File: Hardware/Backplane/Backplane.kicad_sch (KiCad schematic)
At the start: 5 parts, among them U101 P2X8C4M64P, U102 TCA9548APWR

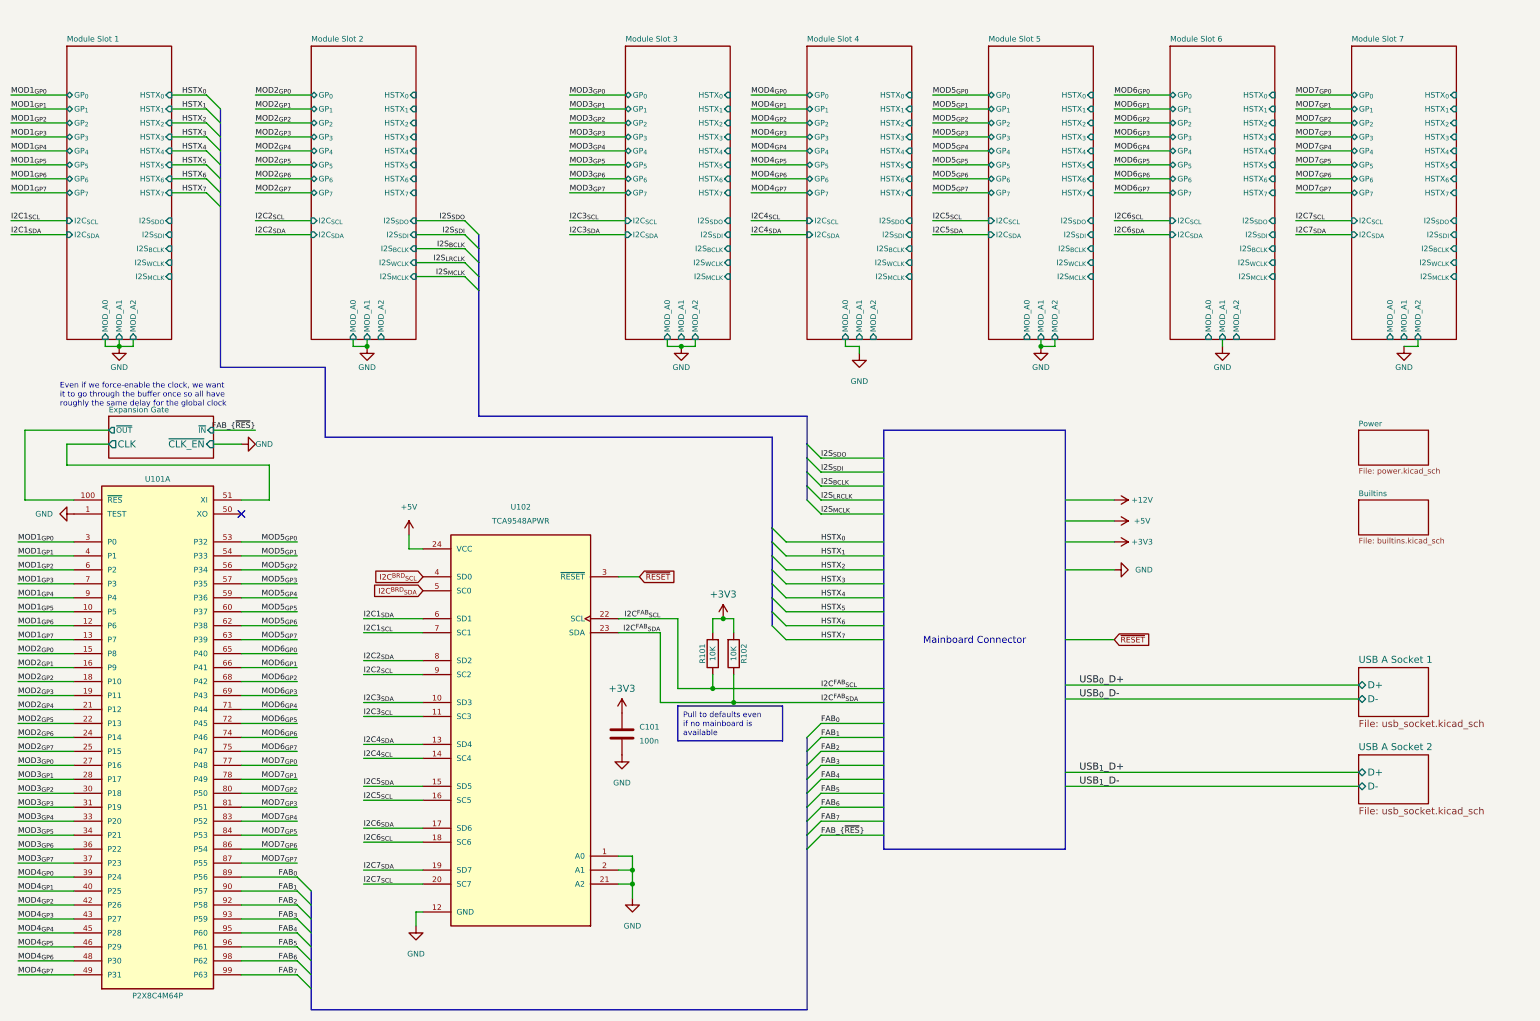
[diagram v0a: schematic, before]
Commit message: Refactors clock system to use AND gates for clock tree spanning and gating.
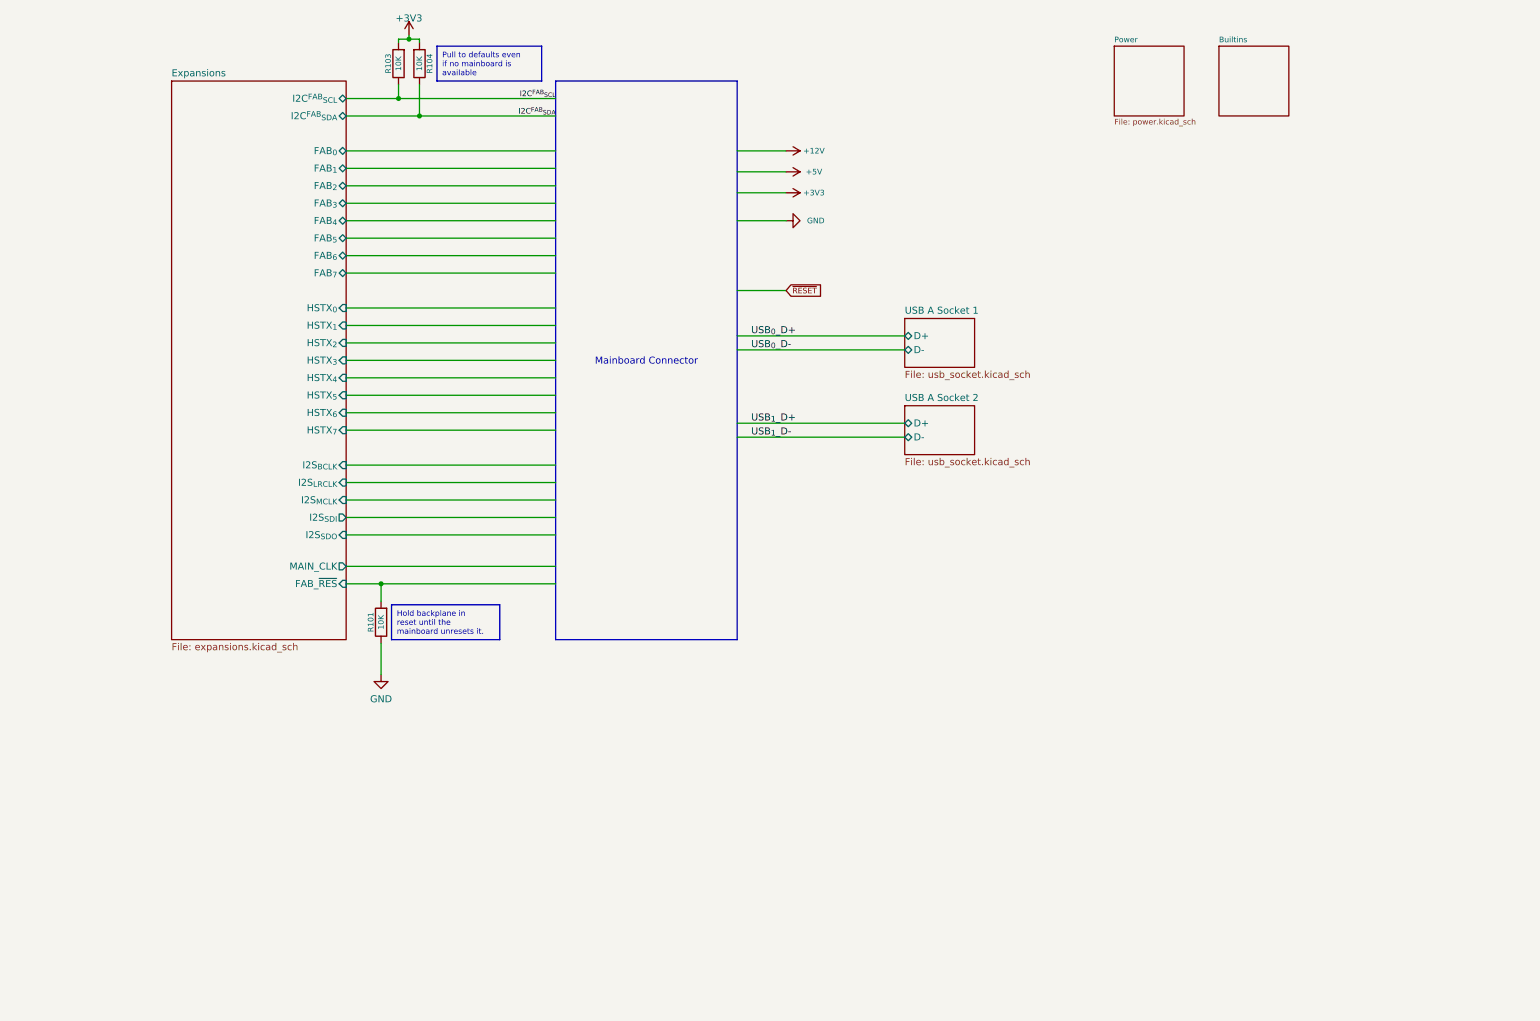
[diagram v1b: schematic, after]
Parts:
- removed C101: 100n, Capacitor_SMD:C_0603_1608Metric, symbol Device:C
- removed R102: 10K, Resistor_SMD:R_0603_1608Metric, symbol Device:R
- removed U101: P2X8C4M64P, Home Computer:QFP50P1600X1600X120-101N, symbol Home Computer:P2X8C4M64P
- removed U102: TCA9548APWR, TCA9548APWR:SOP65P640X120-24N, symbol Home Computer:TCA9548APWR
- added R103, R104: 10K, Resistor_SMD:R_0603_1608Metric, symbol Device:R
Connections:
- net +3V3: now also R103.2, R104.2; no longer R101.2
- net GND: now also R101.1
- net I2C^{FAB}_{SCL}: now also R103.1; no longer R101.1
- net I2C^{FAB}_{SDA}: now also R104.1
- new net Expansions/FAB_~{RES}: R101.2
- no-connect marks 1 -> 0
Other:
- removed sheet Expansion Gate
- removed sheet Module Slot 1
- removed sheet Module Slot 2
- removed sheet Module Slot 3
- removed sheet Module Slot 4
- removed sheet Module Slot 5
- removed sheet Module Slot 6
- removed sheet Module Slot 7
- added sheet Expansions (expansions.kicad_sch)
- note removed: "Even if we force-enable the clock, we want it to go through the buffer once so all have roughly the same delay for the global clock"

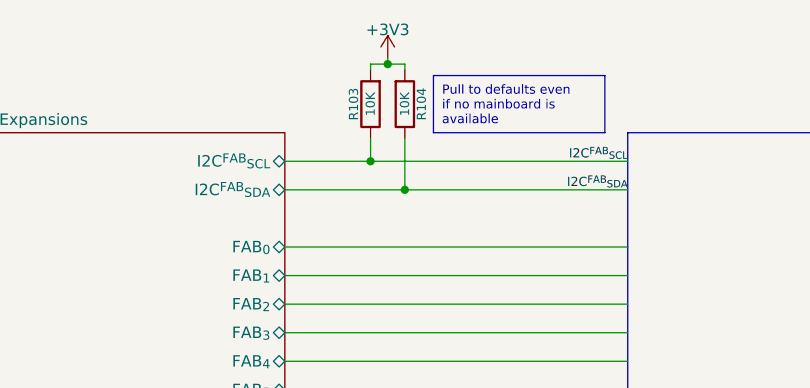
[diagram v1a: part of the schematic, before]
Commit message: Some cleanups of Backplane schematic: Adds DigiKey part numbers, removes unnecessary properties, marks test points as excluded from BOM
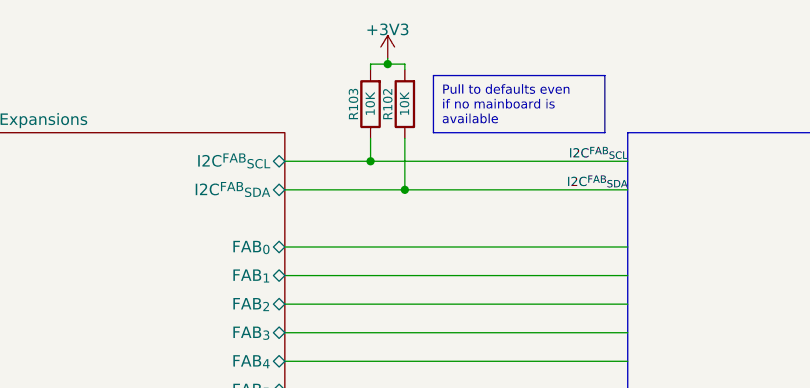
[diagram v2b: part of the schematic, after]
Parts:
- removed R104: 10K, Resistor_SMD:R_0603_1608Metric, symbol Device:R
- added R102: 10K, Resistor_SMD:R_0603_1608Metric, symbol Device:R
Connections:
- net +3V3: now also R102.2
- net I2C^{FAB}_{SDA}: now also R102.1
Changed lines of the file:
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@@
-	(symbol
-		(lib_id "Device:R")
-		(at 89.535 22.225 0)
-		(mirror x)
-		(unit 1)
-		(exclude_from_sim no)
-		(in_bom yes)
-		(on_board yes)
-		(dnp no)
-		(property "Reference" "R104"
-			(at 90.805 22.225 90)
-			(effects
-				(font
-					(size 1.016 1.016)
-				)
-				(justify top)
-			)
-		)
-		(property "Value" "10K"
-			(at 89.535 22.225 90)
-			(effects
-				(font
-					(size 1.016 1.016)
-				)
-			)
-		)
-		(property "Footprint" "Resistor_SMD:R_0603_1608Metric"
-			(at 87.757 22.225 90)
-			(effects
-				(font
-					(size 1.27 1.27)
-				)
-				(hide yes)
-			)
-		)
-		(property "Datasheet" "~"
-			(at 89.535 22.225 0)
-			(effects
-				(font
-					(size 1.27 1.27)
-				)
-				(hide yes)
-			)
-		)
-		(property "Description" "Resistor"
-			(at 89.535 22.225 0)
-			(effects
-				(font
-					(size 1.27 1.27)
-				)
-				(hide yes)
-			)
-		)
-		(pin "1"
-		)
-		(pin "2"
-		)
-		(instances
-			(project "Backplane"
-				(path "/c6da991a-d3ed-4ac1-8b0d-12cd7ba8539b"
-					(reference "R104")
-					(unit 1)
-				)
-			)
-		)
-	)
 	(symbol
 		(lib_id "Device:R")
@@
 			)
 		)
-		(property "Datasheet" "~"
+		(property "Datasheet" ""
 			(at 85.725 22.225 0)
 			(effects
@@
 			)
 		)
-		(property "Datasheet" "~"
+		(property "Datasheet" ""
 			(at 82.55 123.825 0)
 			(effects
@@
 					(unit 1)
 				)
+			)
+		)
+	)
+	(symbol
+		(lib_id "Device:R")
+		(at 89.535 22.225 180)
+		(unit 1)
+		(exclude_from_sim no)
+		(in_bom yes)
+		(on_board yes)
+		(dnp no)
+		(property "Reference" "R102"
+			(at 88.265 22.225 90)
+			(effects
+				(font
+					(size 1.016 1.016)
+				)
+				(justify top)
+			)
+		)
+		(property "Value" "10K"
+			(at 89.535 22.225 90)
+			(effects
+				(font
+					(size 1.016 1.016)
+				)
+			)
+		)
+		(property "Footprint" "Resistor_SMD:R_0603_1608Metric"
+			(at 91.313 22.225 90)
+			(effects
+				(font
+					(size 1.27 1.27)
+				)
+				(hide yes)
+			)
+		)
+		(property "Datasheet" ""
+			(at 89.535 22.225 0)
+			(effects
+				(font
+					(size 1.27 1.27)
+				)
+				(hide yes)
+			)
+		)
+		(property "Description" "Resistor"
+			(at 89.535 22.225 0)
+			(effects
+				(font
+					(size 1.27 1.27)
+				)
+				(hide yes)
+			)
+		)
+		(pin "1"
+		)
+		(pin "2"
+		)
+		(instances
+			(project "Backplane"
+				(path "/c6da991a-d3ed-4ac1-8b0d-12cd7ba8539b"
+					(reference "R102")
+					(unit 1)
+				)

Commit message: Adjusts to review comments
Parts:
- added J101: 10018784-10201TLF, Home Computer:CONN_10018784-10201TLF, symbol Home Computer:10018784-10201TLF
- R101, R102, R103: Digikey Part No (none) -> 311-10.0KHRCT-ND
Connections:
- net +12V: now also J101.B1
- net +3V3: now also J101.B5
- net +5V: now also J101.B3
- net Expansions/FAB_{0}: now also J101.A8
- net Expansions/FAB_{1}: now also J101.A9
- net Expansions/FAB_{2}: now also J101.A10
- net Expansions/FAB_{3}: now also J101.A11
- net Expansions/FAB_{4}: now also J101.A12
- net Expansions/FAB_{5}: now also J101.A13
- net Expansions/FAB_{6}: now also J101.A14
- net Expansions/FAB_{7}: now also J101.A15
- net Expansions/FAB_~{RES}: now also J101.A32
- net Expansions/HSTX_{0}: now also J101.A17
- net Expansions/HSTX_{1}: now also J101.A18
- net Expansions/HSTX_{2}: now also J101.A19
- net Expansions/HSTX_{3}: now also J101.A20
- net Expansions/HSTX_{4}: now also J101.A21
- net Expansions/HSTX_{5}: now also J101.A22
- net Expansions/HSTX_{6}: now also J101.A23
- net Expansions/HSTX_{7}: now also J101.A24
- net Expansions/I2S_{BCLK}: now also J101.A25
- net Expansions/I2S_{LRCLK}: now also J101.A26
- net Expansions/I2S_{MCLK}: now also J101.A27
- net Expansions/I2S_{SDI}: now also J101.A28
- net Expansions/I2S_{SDO}: now also J101.A29
- net Expansions/MAIN_CLK: now also J101.A31
- net GND: now also J101.B12, J101.B2, J101.B4, J101.B6, J101.B9
- net I2C^{FAB}_{SCL}: now also J101.A1
- net I2C^{FAB}_{SDA}: now also J101.A2
- net USB_{0}_D+: now also J101.B7
- net USB_{0}_D-: now also J101.B8
- net USB_{1}_D+: now also J101.B10
- net USB_{1}_D-: now also J101.B11
- net ~{RESET}: now also J101.A16
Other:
- note added: "Mainboard Connector"
- note added: "Programming Edge Conncetor for faster production?"

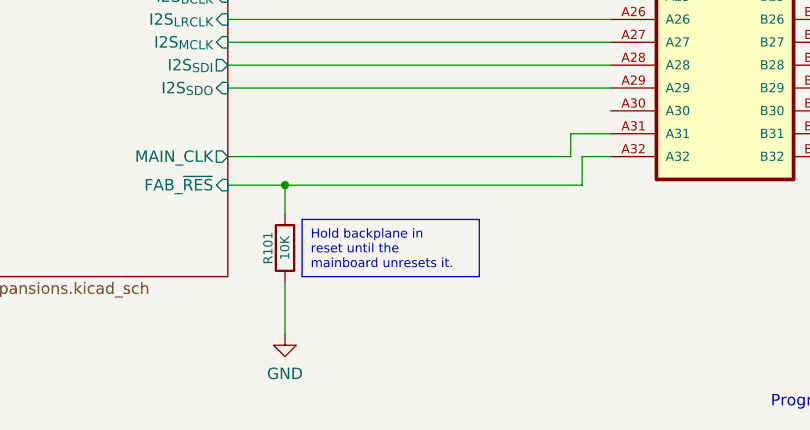
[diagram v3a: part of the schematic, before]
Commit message: Cleans up Backplane schematic even more. Less parts in the BOM, less mistakes!
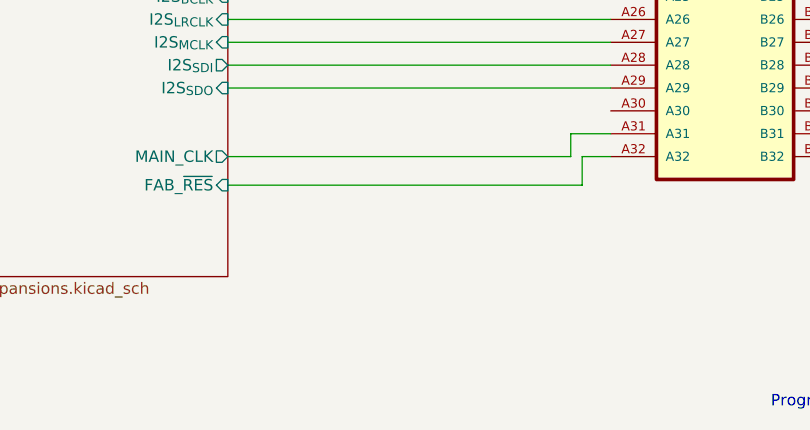
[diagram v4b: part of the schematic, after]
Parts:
- removed R101: 10K, Resistor_SMD:R_0603_1608Metric, symbol Device:R
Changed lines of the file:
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@@
 		)
-	)
-	(text_box "Hold backplane in reset until the mainboard unresets it."
-		(exclude_from_sim no)
-		(at 84.455 120.65 0)
-		(size 19.685 6.35)
-		(margins 0.9525 0.9525 0.9525 0.9525)
-		(stroke
-			(width 0)
-			(type solid)
-		)
-		(fill
-			(type color)
-			(color 255 255 255 1)
-		)
-		(effects
-			(font
-				(size 1.016 1.016)
-			)
-			(justify left top)
-		)
-	)
-	(junction
-		(at 82.55 116.84)
-		(diameter 0)
-		(color 0 0 0 0)
 	)
 	(junction
@@
 	(wire
 		(pts
-			(xy 82.55 116.84) (xy 115.57 116.84)
+			(xy 76.2 116.84) (xy 115.57 116.84)
 		)
 		(stroke
@@
 	(wire
 		(pts
-			(xy 82.55 116.84) (xy 82.55 120.015)
-		)
-		(stroke
-			(width 0)
-			(type default)
-		)
-	)
-	(wire
-		(pts
 			(xy 144.145 57.785) (xy 197.485 57.785)
 		)
@@
 	(wire
 		(pts
-			(xy 82.55 133.35) (xy 82.55 127.635)
-		)
-		(stroke
-			(width 0)
-			(type default)
-		)
-	)
-	(wire
-		(pts
 			(xy 144.145 32.385) (xy 153.035 32.385)
 		)
@@
 		(pts
 			(xy 118.745 113.665) (xy 115.57 113.665)
-		)
-		(stroke
-			(width 0)
-			(type default)
-		)
-	)
-	(wire
-		(pts
-			(xy 76.2 116.84) (xy 82.55 116.84)
 		)
 		(stroke
@@
 				(path "/c6da991a-d3ed-4ac1-8b0d-12cd7ba8539b"
 					(reference "R103")
-					(unit 1)
-				)
-			)
-		)
-	)
-	(symbol
-		(lib_id "power:GND")
-		(at 82.55 133.35 0)
-		(unit 1)
-		(exclude_from_sim no)
-		(in_bom yes)
-		(on_board yes)
-		(dnp no)
-		(fields_autoplaced yes)
-		(property "Reference" "#PWR0107"
-			(at 82.55 139.7 0)
-			(effects
-				(font
-					(size 1.27 1.27)
-				)
-				(hide yes)
-			)
-		)
-		(property "Value" "GND"
-			(at 82.55 137.795 0)
-			(effects
-				(font
-					(size 1.27 1.27)
-				)
-			)
-		)
-		(property "Footprint" ""
-			(at 82.55 133.35 0)
-			(effects
-				(font
-					(size 1.27 1.27)
-				)
-				(hide yes)
-			)
-		)
-		(property "Datasheet" ""
-			(at 82.55 133.35 0)
-			(effects
-				(font
-					(size 1.27 1.27)
-				)
-				(hide yes)
-			)
-		)
-		(property "Description" "Power symbol creates a global label with name \"GND\" , ground"
-			(at 82.55 133.35 0)
-			(effects
-				(font
-					(size 1.27 1.27)
-				)
-				(hide yes)
-			)
-		)
-		(pin "1"
-		)
-		(instances
-			(project ""
-				(path "/c6da991a-d3ed-4ac1-8b0d-12cd7ba8539b"
-					(reference "#PWR0107")
 					(unit 1)
 				)
@@
 					(unit 1)
 				)
-			)
-		)
-	)
-	(symbol
-		(lib_id "Device:R")
-		(at 82.55 123.825 180)
-		(unit 1)
-		(exclude_from_sim no)
-		(in_bom yes)
-		(on_board yes)
-		(dnp no)
-		(property "Reference" "R101"
-			(at 81.28 123.825 90)
-			(effects
-				(font
-					(size 1.016 1.016)
-				)
-				(justify top)
-			)
-		)
-		(property "Value" "10K"
-			(at 82.55 123.825 90)
-			(effects
-				(font
-					(size 1.016 1.016)
-				)
-			)
-		)
-		(property "Footprint" "Resistor_SMD:R_0603_1608Metric"
-			(at 84.328 123.825 90)
-			(effects
-				(font
-					(size 1.27 1.27)
-				)
-				(hide yes)
-			)
-		)
-		(property "Datasheet" "https://www.yageogroup.com/content/datasheet/asset/file/PYU-RC_GROUP_51_ROHS_L"
-			(at 82.55 123.825 0)
-			(effects
-				(font
-					(size 1.27 1.27)
-				)
-				(hide yes)
-			)
-		)
-		(property "Description" "Resistor"
-			(at 82.55 123.825 0)
-			(effects
-				(font
-					(size 1.27 1.27)
-				)
-				(hide yes)
-			)
-		)
-		(property "Digikey Part No" "311-10.0KHRCT-ND"
-			(at 82.55 123.825 90)
-			(effects
-				(font
-					(size 1.27 1.27)
-				)
-				(hide yes)
-			)
-		)
-		(pin "1"
-		)
-		(pin "2"
-		)
-		(instances
-			(project "Backplane"
-				(path "/c6da991a-d3ed-4ac1-8b0d-12cd7ba8539b"
-					(reference "R101")
-					(unit 1)
-				)
